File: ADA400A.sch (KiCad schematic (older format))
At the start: 95 parts, among them J1 BNC, J2 COAX CABLE, K1 TF2E-5V, Q1 Q_PJFET_GSD, Q2 Q_PJFET_GSD, Q3 Q_NPN_BCE, SW1 MSSA2350G, SW2 MSS-2250G, SW3 MSSA4450G, SW4 MSSA4450G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

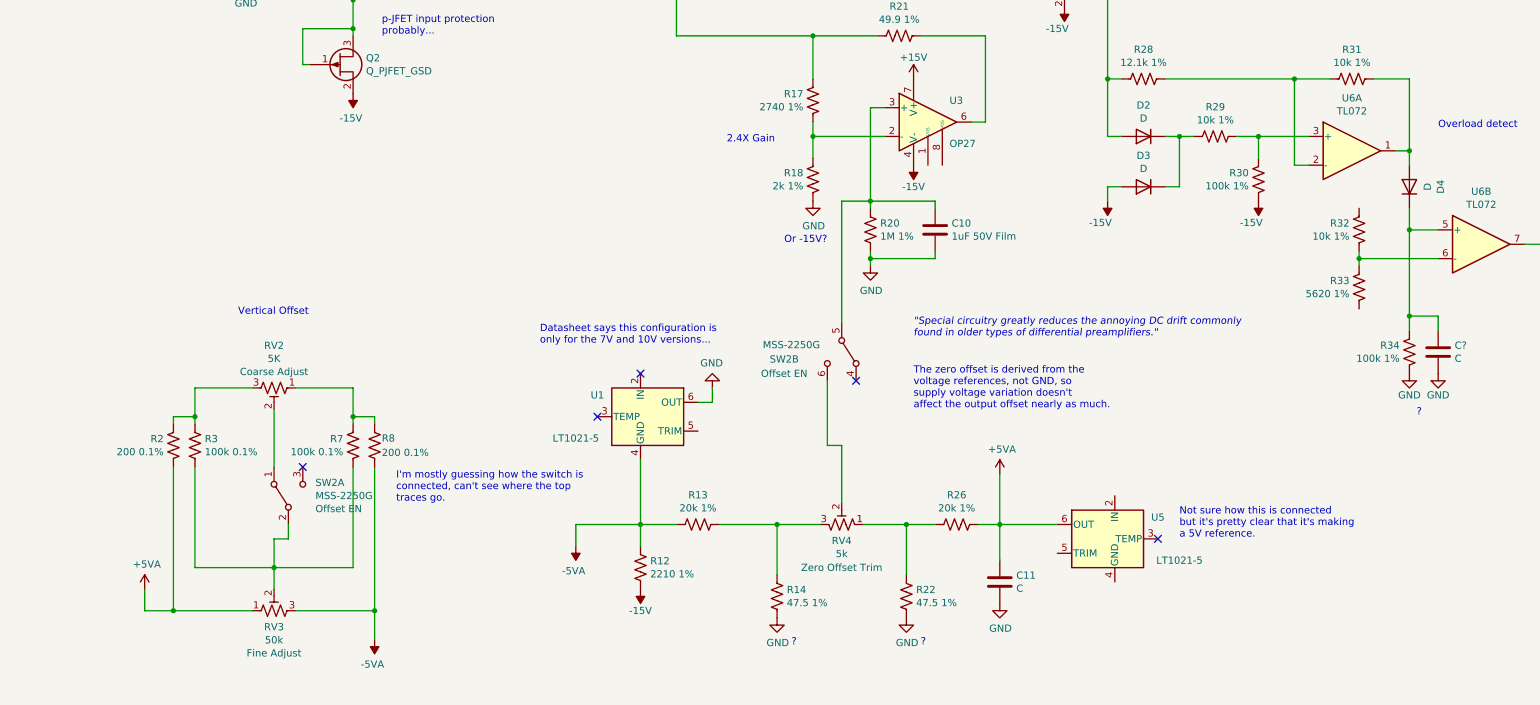
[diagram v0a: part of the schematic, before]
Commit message: Fix connection of offset adjustment
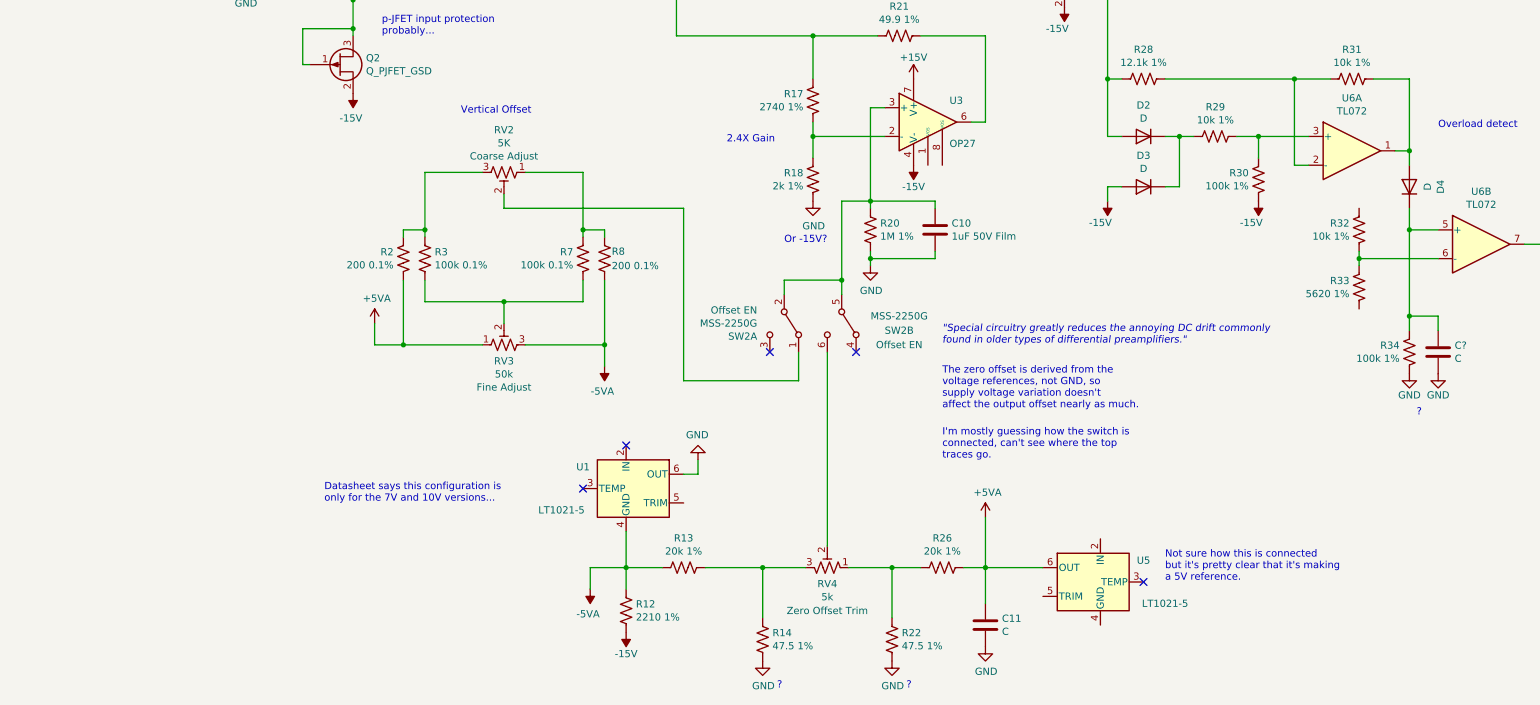
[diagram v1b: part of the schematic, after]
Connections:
- net at R3.2, R7.1, RV3.2: no longer SW2.2 (B)
- net at C10.1, R20.2, SW2.5 (B)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: now also SW2.2 (B)
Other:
- moved on the sheet: C11, R12, R13, R14, R2, R22, R26, R3, R7, R8, RV2, RV3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

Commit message: Diode-connected JFETs, duh
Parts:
- removed Q1, Q2: Q_PJFET_GSD, symbol Device:Q_PJFET_GSD
- added Q1, Q2: NJFET, Package_TO_SOT_SMD:SOT-23, symbol Transistor_FET:BF545A
- gave numbers to parts that had none: 1
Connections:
- net +15V: now also Q1.1 (S), Q1.2 (D)
- net -15V: now also Q2.3 (G)
- net at R10.2, U2.2 (-): now also Q1.3 (G), Q2.1 (S), Q2.2 (D)
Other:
- note added: "Unknown Tek-numbered TO92s.\nProbably diode-connected JFETs."
- note removed: "p-JFET input protection\nprobably..."
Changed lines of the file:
@@
 Connection ~ 5700 7450
-$Comp
-L Device:Q_PJFET_GSD Q1
-U 1 1 617D7EAB
-P 3850 4700
-F 0 "Q1" H 4040 4746 50  0000 L CNN
-F 1 "Q_PJFET_GSD" H 4040 4655 50  0000 L CNN
-F 2 "" H 4050 4800 50  0001 C CNN
-F 3 "~" H 3850 4700 50  0001 C CNN
-	1    3850 4700
-	1    0    0    -1
-$EndComp
-$Comp
-L Device:Q_PJFET_GSD Q2
-U 1 1 617EC9DD
-P 3850 5500
-F 0 "Q2" H 4040 5546 50  0000 L CNN
-F 1 "Q_PJFET_GSD" H 4040 5455 50  0000 L CNN
-F 2 "" H 4050 5600 50  0001 C CNN
-F 3 "~" H 3850 5500 50  0001 C CNN
-	1    3850 5500
-	1    0    0    -1
-$EndComp
-Wire Wire Line
-	3950 5300 3950 5250
-Wire Wire Line
-	3650 5500 3600 5500
-Wire Wire Line
-	3600 5500 3600 5250
-Wire Wire Line
-	3600 5250 3950 5250
-Connection ~ 3950 5250
-Wire Wire Line
-	3950 5250 3950 5050
 $Comp
 L power:-15V #PWR09
 U 1 1 61813805
-P 3950 5700
-F 0 "#PWR09" H 3950 5800 50  0001 C CNN
-F 1 "-15V" H 3965 5873 50  0000 C CNN
-F 2 "" H 3950 5700 50  0001 C CNN
-F 3 "" H 3950 5700 50  0001 C CNN
-	1    3950 5700
+P 3950 5750
+F 0 "#PWR09" H 3950 5850 50  0001 C CNN
+F 1 "-15V" H 3965 5923 50  0000 C CNN
+F 2 "" H 3950 5750 50  0001 C CNN
+F 3 "" H 3950 5750 50  0001 C CNN
+	1    3950 5750
 	-1   0    0    1
 $EndComp
@@
 L power:+15V #PWR08
 U 1 1 61813C8A
-P 3950 4350
-F 0 "#PWR08" H 3950 4200 50  0001 C CNN
-F 1 "+15V" H 3965 4523 50  0000 C CNN
-F 2 "" H 3950 4350 50  0001 C CNN
-F 3 "" H 3950 4350 50  0001 C CNN
-	1    3950 4350
-	1    0    0    -1
-$EndComp
-Wire Wire Line
-	3950 4350 3950 4450
-Wire Wire Line
-	3950 4450 3600 4450
-Wire Wire Line
-	3600 4450 3600 4700
-Wire Wire Line
-	3600 4700 3650 4700
-Connection ~ 3950 4450
-Wire Wire Line
-	3950 4450 3950 4500
+P 3950 4400
+F 0 "#PWR08" H 3950 4250 50  0001 C CNN
+F 1 "+15V" H 3965 4573 50  0000 C CNN
+F 2 "" H 3950 4400 50  0001 C CNN
+F 3 "" H 3950 4400 50  0001 C CNN
+	1    3950 4400
+	1    0    0    -1
+$EndComp
 Wire Wire Line
 	4300 3800 4300 3850
@@
 	4300 3850 5800 3850
 Wire Wire Line
-	3950 5050 4300 5050
-Wire Wire Line
-	4300 5050 4300 3850
-Connection ~ 3950 5050
-Wire Wire Line
-	3950 5050 3950 4900
+	3950 5100 4300 5100
+Wire Wire Line
+	4300 5100 4300 3850
 Connection ~ 4300 3850
-Text Notes 4150 5300 0    50   ~ 0
-p-JFET input protection\nprobably...
 $Comp
 L power:GND #PWR028
@@
 	11300 7250 11300 7350
 $Comp
-L Device:C C?
+L Device:C C18
 U 1 1 6241EAB8
 P 11500 7500
-F 0 "C?" H 11615 7546 50  0000 L CNN
+F 0 "C18" H 11615 7546 50  0000 L CNN
 F 1 "C" H 11615 7455 50  0000 L CNN
 F 2 "" H 11538 7350 50  0001 C CNN
@@
 $EndComp
 $Comp
-L power:GND #PWR?
+L power:GND #PWR06
 U 1 1 6241F5C1
 P 11300 7650
-F 0 "#PWR?" H 11300 7400 50  0001 C CNN
+F 0 "#PWR06" H 11300 7400 50  0001 C CNN
 F 1 "GND" H 11300 7500 50  0000 C CNN
 F 2 "" H 11300 7650 50  0001 C CNN
@@
 $EndComp
 $Comp
-L power:GND #PWR?
+L power:GND #PWR038
 U 1 1 62436D56
 P 11500 7650
-F 0 "#PWR?" H 11500 7400 50  0001 C CNN
+F 0 "#PWR038" H 11500 7400 50  0001 C CNN
 F 1 "GND" H 11500 7500 50  0000 C CNN
 F 2 "" H 11500 7650 50  0001 C CNN
@@
 Wire Wire Line
 	7050 7700 7050 7500
+$Comp
+L Transistor_FET:BF545A Q1
+U 1 1 607F5050
+P 3950 4800
+F 0 "Q1" V 3950 5050 50  0000 C CNN
+F 1 "NJFET" V 4187 4800 50  0000 C CNN
+F 2 "Package_TO_SOT_SMD:SOT-23" H 4150 4725 50  0001 L CIN
+F 3 "https://www.nxp.com/docs/en/data-sheet/BF545A_BF545B_BF545C.pdf" H 3950 4800 50  0001 L CNN
+	1    3950 4800
+	0    -1   -1   0
+$EndComp
+Wire Wire Line
+	3950 5000 3950 5100
+Wire Wire Line
+	3750 4700 3750 4450
+Wire Wire Line
+	3750 4450 3950 4450
+Wire Wire Line
+	3950 4450 3950 4400
+Wire Wire Line
+	3950 4450 4150 4450
+Wire Wire Line
+	4150 4450 4150 4700
+Connection ~ 3950 4450
+$Comp
+L Transistor_FET:BF545A Q2
+U 1 1 608BC4AA
+P 3950 5550
+F 0 "Q2" V 3950 5800 50  0000 C CNN
+F 1 "NJFET" V 4187 5550 50  0000 C CNN
+F 2 "Package_TO_SOT_SMD:SOT-23" H 4150 5475 50  0001 L CIN
+F 3 "https://www.nxp.com/docs/en/data-sheet/BF545A_BF545B_BF545C.pdf" H 3950 5550 50  0001 L CNN
+	1    3950 5550
+	0    -1   -1   0
+$EndComp
+Wire Wire Line
+	3750 5450 3750 5200
+Wire Wire Line
+	3750 5200 3950 5200
+Wire Wire Line
+	4150 5200 4150 5450
+Wire Wire Line
+	3950 5100 3950 5200
+Connection ~ 3950 5100
+Connection ~ 3950 5200
+Wire Wire Line
+	3950 5200 4150 5200
+Text Notes 4350 5100 0    50   ~ 0
+Unknown Tek-numbered TO92s.\nProbably diode-connected JFETs.
 $EndSCHEMATC
